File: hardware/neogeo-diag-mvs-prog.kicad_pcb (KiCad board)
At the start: 2 copper layers, 174 x 134 mm, 21 parts, among them J1 NeoGeo MVS Prog B Side Edge, J2 NeoGeo MVS Prog A Side Edge, J3 NeoGeo MVS Prog B Side Edge, J4 NeoGeo MVS Prog A Side Edge, U1 AS6C8016, U2 74LS11, U3 74LS08, U4 74LS04

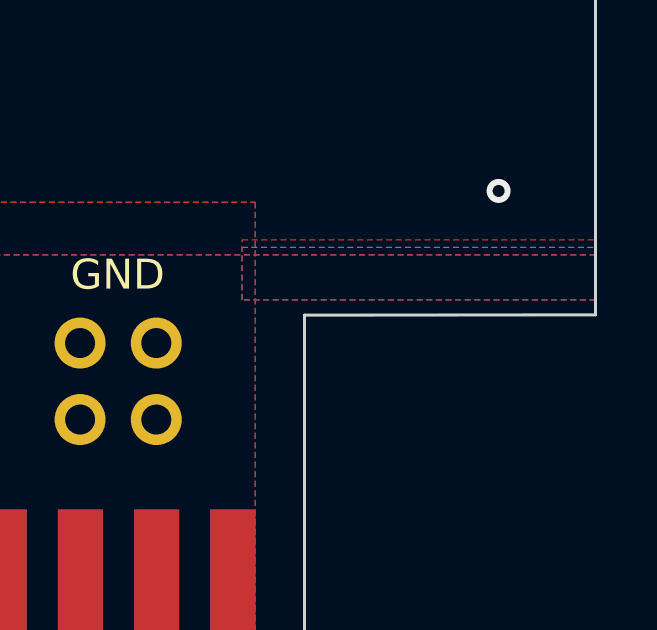
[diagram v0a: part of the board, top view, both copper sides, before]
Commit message: Fixes: directions in schematic, non-straight edge-cut
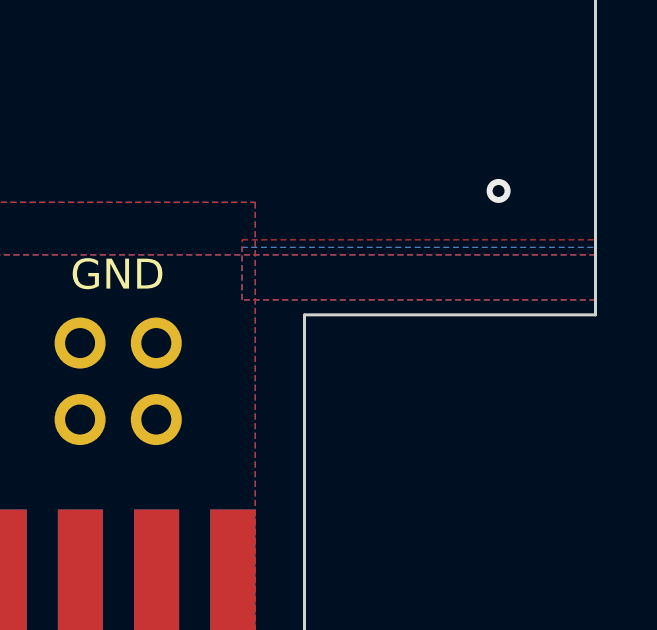
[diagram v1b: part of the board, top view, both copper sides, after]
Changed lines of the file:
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@@
   (gr_line (start 190.75 23.75) (end 190.75 26.25) (layer "Edge.Cuts") (width 0.1))
   (gr_line (start 52.75 23.75) (end 88.75 23.75) (layer "Edge.Cuts") (width 0.1))
-  (gr_line (start 217.05 138.76) (end 226.75 138.75) (layer "Edge.Cuts") (width 0.1))
+  (gr_line (start 217.05 138.75) (end 226.75 138.75) (layer "Edge.Cuts") (width 0.1))
   (gr_circle (center 94.75 127) (end 99.75 127) (layer "Edge.Cuts") (width 0.1) (fill none))
   (gr_line (start 226.75 23.75) (end 190.75 23.75) (layer "Edge.Cuts") (width 0.1))
